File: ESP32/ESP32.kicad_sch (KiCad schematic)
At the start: 52 parts, among them J1 104031-0811, P1 USB_C_Plug_USB2.0, Q1 S8050, Q2 S8050, U1 ESP32-S3, U2 W25Q128JV, U3 APS1604M-3SQRx-SN, U5 AMS1117, U6 CH340C, U7 USBLC6-2SC6, Y1 Crystal, Y2 Crystal

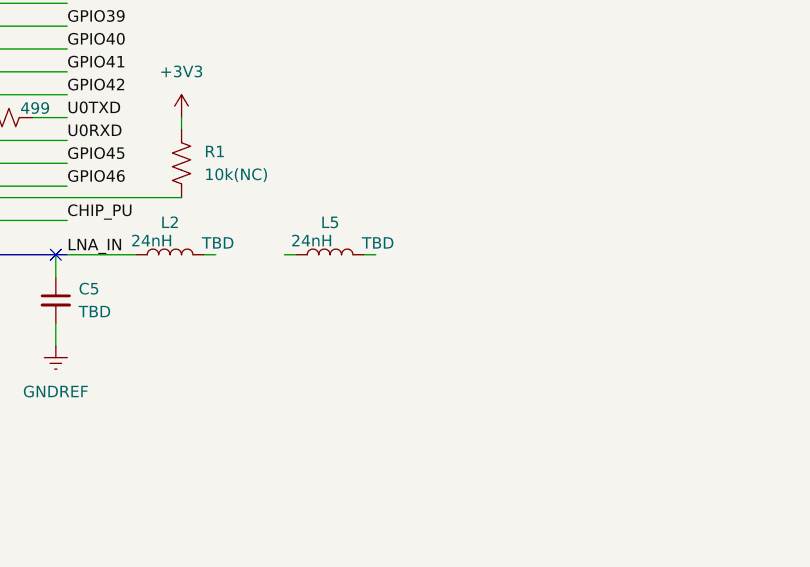
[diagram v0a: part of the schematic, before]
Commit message: ESP32-S3 New Version
V10
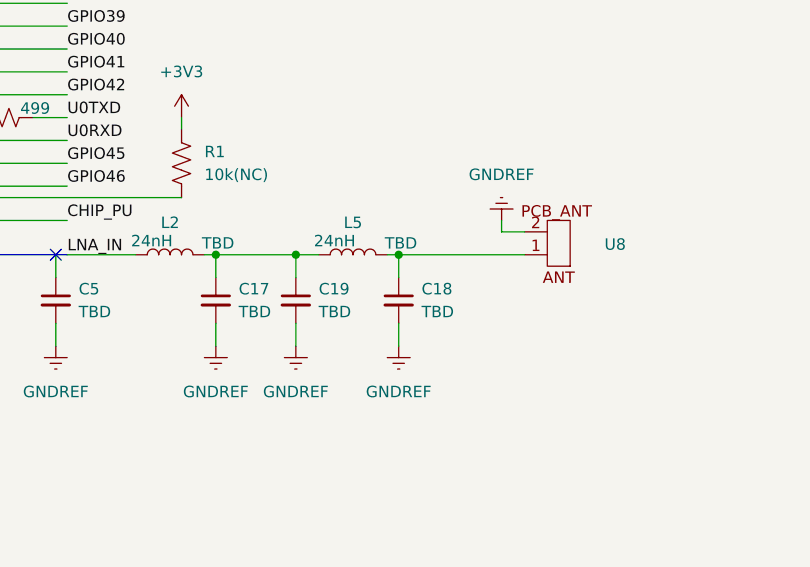
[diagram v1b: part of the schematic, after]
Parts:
- added C17, C18, C19: TBD, symbol Device:C_Small
- added U8: (no value), symbol ESP32_sym:PCB_ANT
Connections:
- net GND: now also C17.2, C18.2, C19.2, U8.2
- net at L2.2: now also L5.1, C17.1, C19.1
- net at L5.2: now also C18.1, U8.1
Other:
- moved on the sheet: L5
